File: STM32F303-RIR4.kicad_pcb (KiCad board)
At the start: 2 copper layers, 73.7 x 106.7 mm, 10 parts, among them J0 CN7, J1 CN10, J101 LCC, J102 LCC, U101 SN65HVD1050

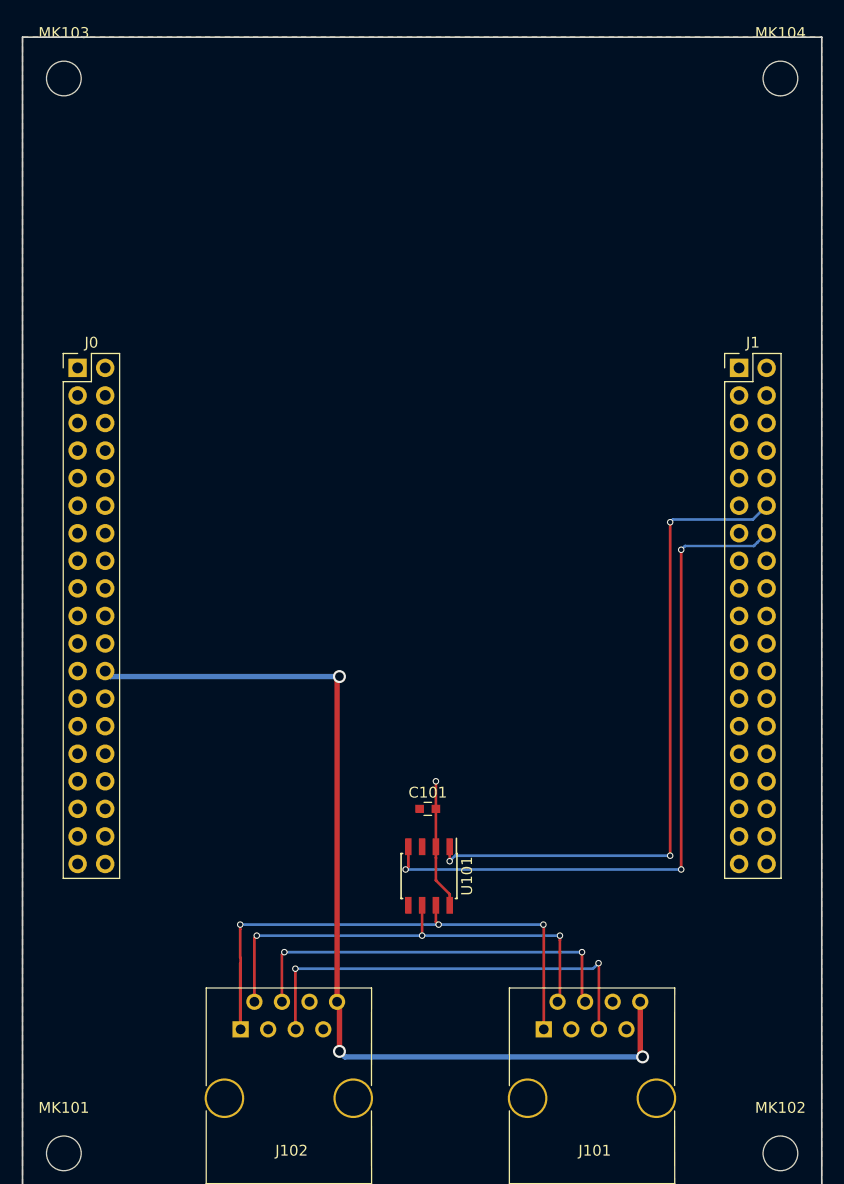
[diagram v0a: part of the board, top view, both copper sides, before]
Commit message: Add activity LEDS.
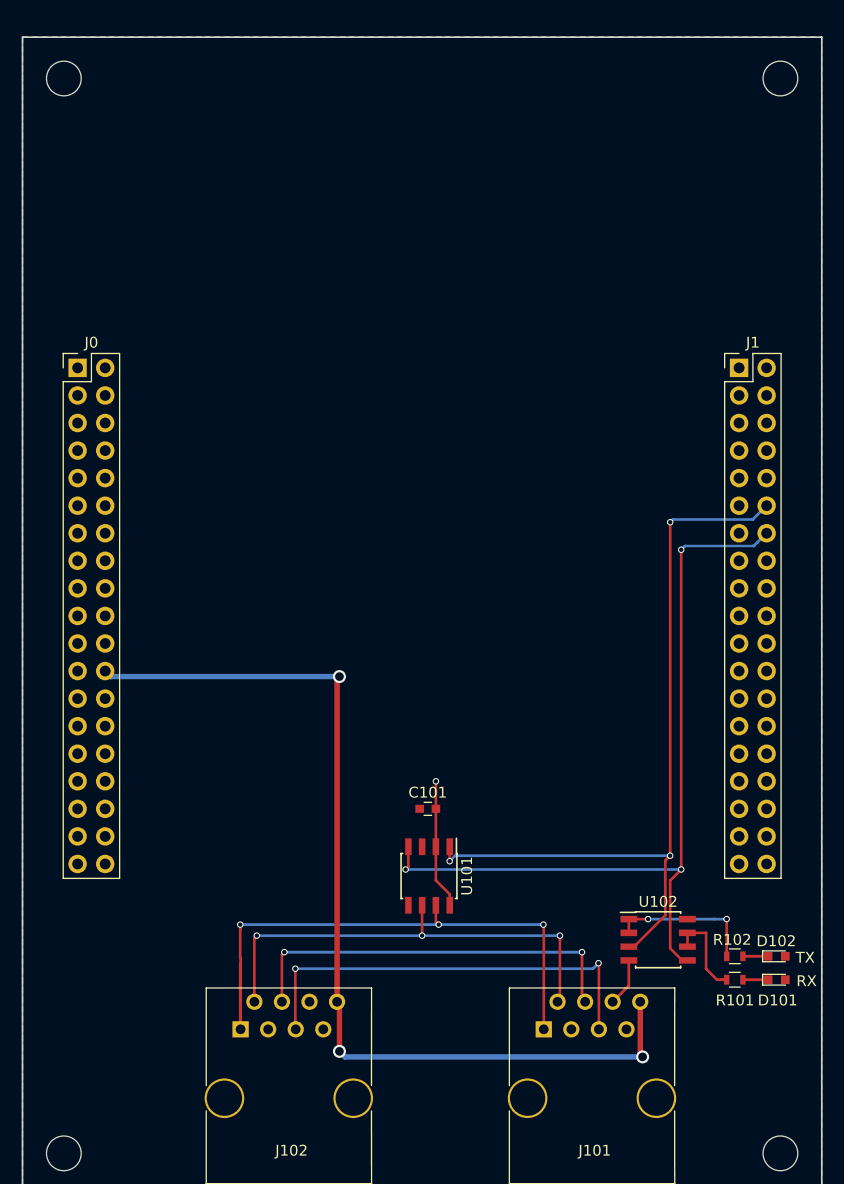
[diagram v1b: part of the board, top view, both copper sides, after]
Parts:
- added D101: RX, LEDs:LED_0603, F.Cu at (182.5, 158.0)
- added D102: TX, LEDs:LED_0603, F.Cu at (182.5, 155.8)
- added R101: 390, Resistors_SMD:R_0603, F.Cu at (178.7, 158.0)
- added R102: 390, Resistors_SMD:R_0603, F.Cu at (178.7, 155.8)
- added U102: LM358, Housings_SOIC:SOIC-8_3.9x4.9mm_Pitch1.27mm, F.Cu at (171.6, 154.3)
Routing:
- net Net-(R102-Pad2): track 0.00 -> 13.7 mm, vias 0 -> 2
- net /CAN_TX: track 62.1 -> 72.4 mm
- net /CAN_RX: track 65.6 -> 75.3 mm
- net Net-(R101-Pad2): track 0.00 -> 8.86 mm
- net GND: track 12.0 -> 16.4 mm
- net Net-(D102-Pad1): track 0.00 -> 2.31 mm
- net Net-(D101-Pad1): track 0.00 -> 2.31 mm

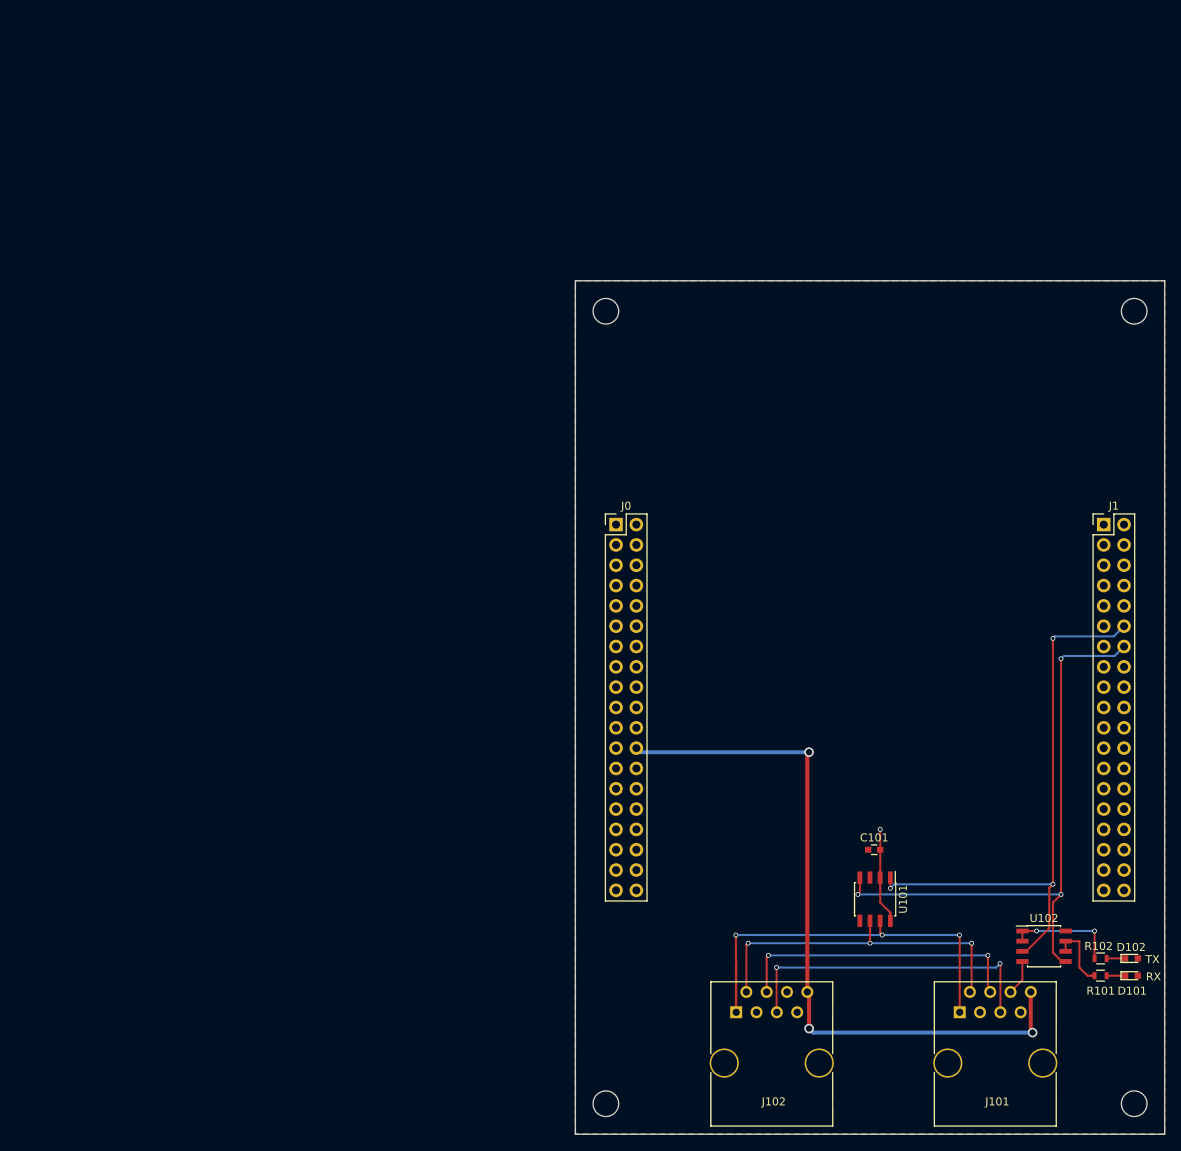
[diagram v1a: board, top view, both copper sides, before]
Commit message: Final tweaks to the board, added labels and logos.
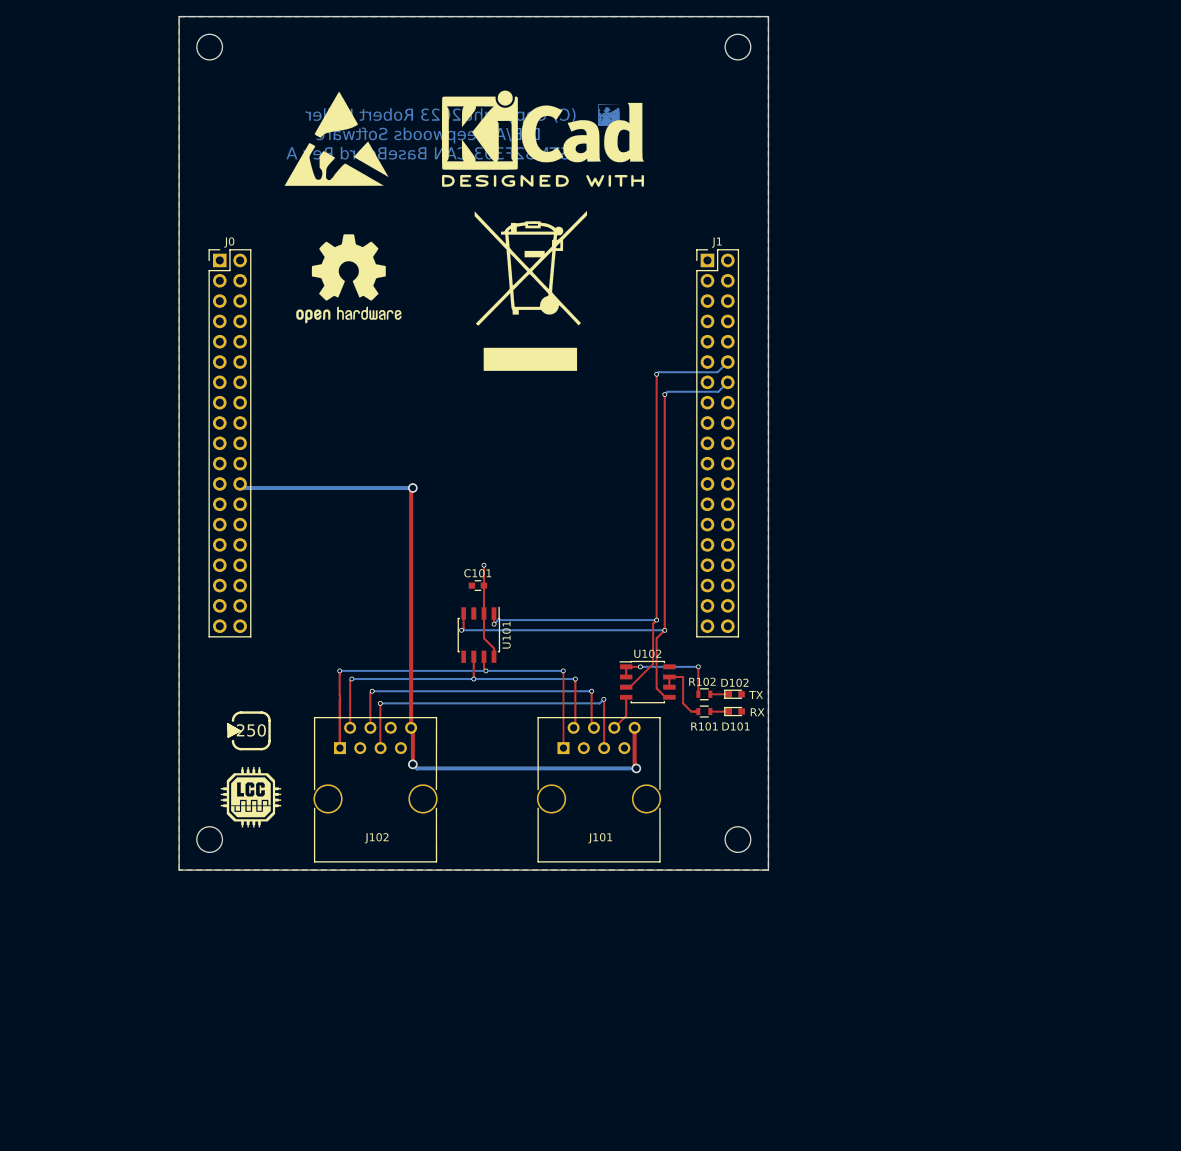
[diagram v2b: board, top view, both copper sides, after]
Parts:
- added ?: , DWSLogoBCU:DWSLogoBCU, F.Cu at (117.2, 50.4)
- added G***: LCC, LCC_LOGO:LCC_LOGO_9x9, F.Cu at (72.5, 135.6)
- added REF**: PowerLabel-250, PowerLabels:PowerLabel-250, F.Cu at (72.5, 127.4)
- added REF***: ESD-Logo_13.2x12mm_SilkScreen, Symbols:ESD-Logo_13.2x12mm_SilkScreen, F.Cu at (83.2, 53.3)
- added REF***: KiCad-Logo2_12mm_SilkScreen, Symbols:KiCad-Logo2_12mm_SilkScreen, F.Cu at (109.0, 53.3)
- added REF***: OSHW-Logo2_14.6x12mm_SilkScreen, Symbols:OSHW-Logo2_14.6x12mm_SilkScreen, F.Cu at (84.7, 70.9)
- added REF***: WEEE-Logo_14x20mm_SilkScreen, Symbols:WEEE-Logo_14x20mm_SilkScreen, F.Cu at (107.4, 72.4)
- moved U102 59.5 mm to (122.1, 121.3)
- moved C101 59.5 mm to (100.8, 109.2)
- moved D102 59.5 mm to (133.0, 122.8)
- moved J102 59.5 mm to (83.6, 129.5)
- moved MK101 59.5 mm to (67.3, 141.0)
- moved MK102 59.5 mm to (133.3, 141.0)
- moved MK103 59.5 mm to (67.3, 41.9)
- moved MK104 59.5 mm to (133.3, 41.9)
- moved R102 59.5 mm to (129.1, 122.8)
- moved U101 59.5 mm to (101.0, 115.4)
- moved J101 59.5 mm to (111.5, 129.5)
- moved D101 59.5 mm to (133.0, 125.0)
- moved J0 59.5 mm to (68.6, 68.6)
- moved J1 59.5 mm to (129.5, 68.6)
- moved R101 59.5 mm to (129.1, 125.0)
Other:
- board text added: "(C) Copyright 2023 Robert Heller D/B/A Deepwoods Software STM32F303 CAN BaseBoard Rev A"

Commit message: Add additional outputs (crossing controls).
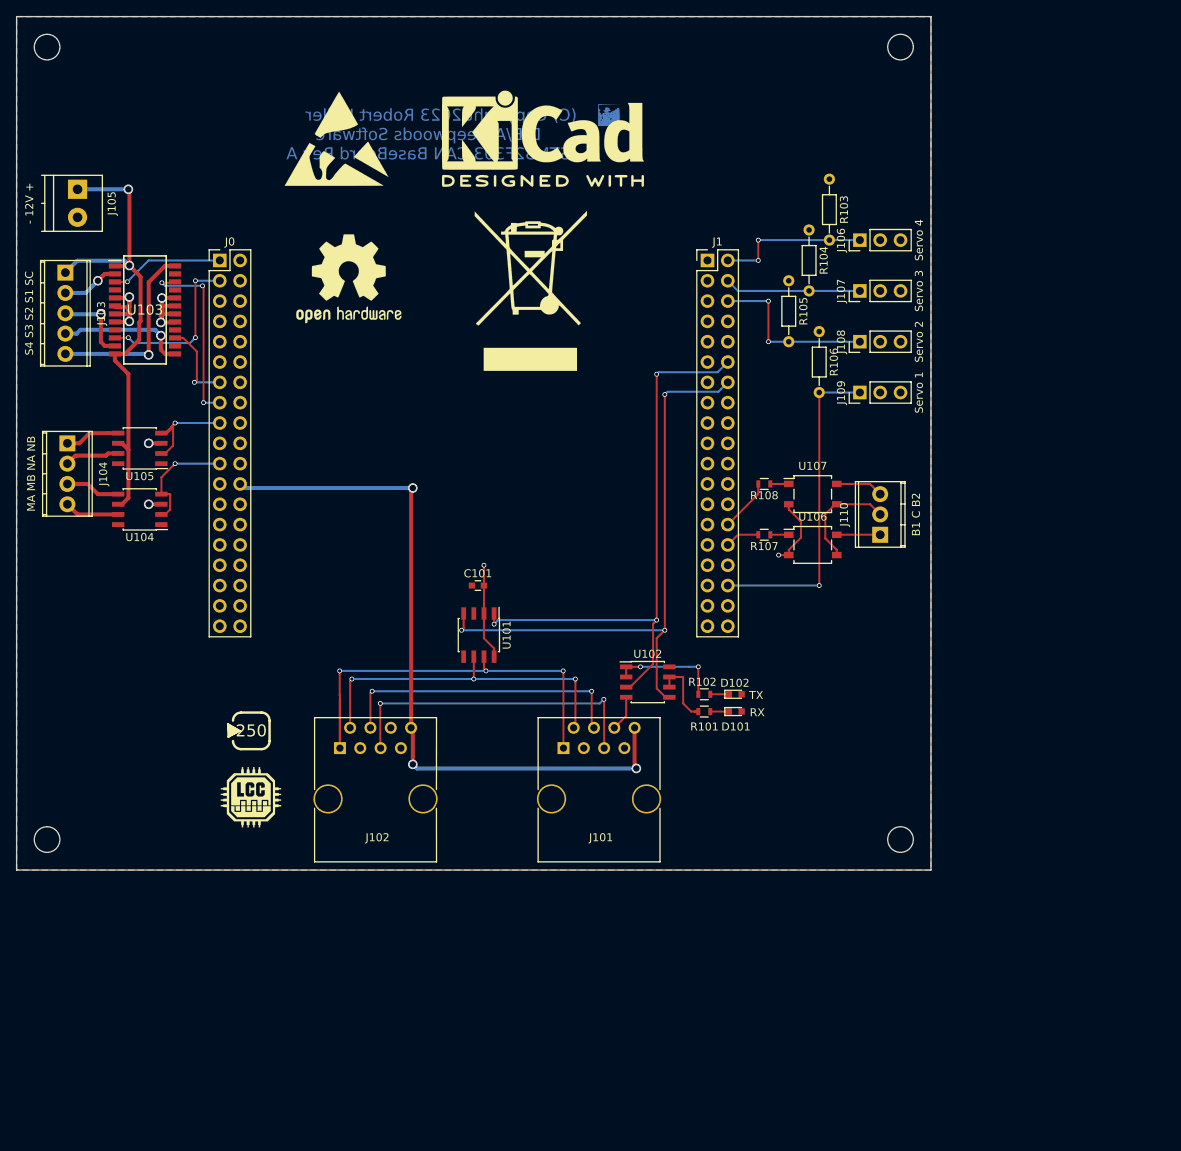
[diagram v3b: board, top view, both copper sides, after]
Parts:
- added J103: S4 S3 S2 S1 SC, Terminal_Blocks:TerminalBlock_Pheonix_MPT-2.54mm_5pol, F.Cu at (49.3, 70.1)
- added J104: MA MB NA NB, Terminal_Blocks:TerminalBlock_Pheonix_MPT-2.54mm_4pol, F.Cu at (49.5, 91.4)
- added J105: - 12V +, Terminal_Blocks:TerminalBlock_Pheonix_PT-3.5mm_2pol, F.Cu at (50.8, 59.7)
- added J106: Servo 4, Pin_Headers:Pin_Header_Straight_1x03_Pitch2.54mm, F.Cu at (148.6, 66.0)
- added J107: Servo 3, Pin_Headers:Pin_Header_Straight_1x03_Pitch2.54mm, F.Cu at (148.6, 72.4)
- added J108: Servo 2, Pin_Headers:Pin_Header_Straight_1x03_Pitch2.54mm, F.Cu at (148.6, 78.7)
- added J109: Servo 1, Pin_Headers:Pin_Header_Straight_1x03_Pitch2.54mm, F.Cu at (148.6, 85.1)
- added J110: B1 C B2, Terminal_Blocks:TerminalBlock_Pheonix_MPT-2.54mm_3pol, F.Cu at (151.1, 102.9)
- added R103: 5K to 20K, Resistors_THT:R_Axial_DIN0204_L3.6mm_D1.6mm_P7.62mm_Horizontal, F.Cu at (144.8, 58.4)
- added R104: 5K to 20K, Resistors_THT:R_Axial_DIN0204_L3.6mm_D1.6mm_P7.62mm_Horizontal, F.Cu at (142.2, 64.8)
- added R105: 5K to 20K, Resistors_THT:R_Axial_DIN0204_L3.6mm_D1.6mm_P7.62mm_Horizontal, F.Cu at (139.7, 71.1)
- added R106: 5K to 20K, Resistors_THT:R_Axial_DIN0204_L3.6mm_D1.6mm_P7.62mm_Horizontal, F.Cu at (143.5, 77.5)
- added R107: 330, Resistors_SMD:R_0603, F.Cu at (136.6, 102.9)
- added R108: 330, Resistors_SMD:R_0603, F.Cu at (136.6, 96.5)
- added U103: TBD62064AFG, SOP100P800X190:SOP100P800X190-24N, F.Cu at (59.2, 74.8)
- added U104: TC4428, Housings_SOIC:SOIC-8_3.9x4.9mm_Pitch1.27mm, F.Cu at (58.6, 99.7)
- added U105: TC4428, Housings_SOIC:SOIC-8_3.9x4.9mm_Pitch1.27mm, F.Cu at (58.6, 92.1)
- added U106: G3VM-61VY4, Housings_SOIC:SO-4_4.4x4.3mm_Pitch2.54mm, F.Cu at (142.7, 104.1)
- added U107: G3VM-61VY4, Housings_SOIC:SO-4_4.4x4.3mm_Pitch2.54mm, F.Cu at (142.7, 97.8)
- moved MK101 20.3 mm to (47.0, 141.0)
- moved MK103 20.3 mm to (47.0, 41.9)
- moved MK102 20.3 mm to (153.7, 141.0)
- moved MK104 20.3 mm to (153.7, 41.9)
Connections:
- J1 pad 2: Net-(J1-Pad2) -> /Servo4
- J1 pad 28: Net-(J1-Pad28) -> /SSR2
- J1 pad 30: Net-(J1-Pad30) -> /SSR1
- J1 pad 34: Net-(J1-Pad34) -> /Servo1
- J1 pad 4: Net-(J1-Pad4) -> /Servo3
- J1 pad 6: Net-(J1-Pad6) -> /Servo2
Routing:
- net +12V: track 0.00 -> 62.2 mm, vias 0 -> 2
- net /Servo1: track 0.00 -> 40.6 mm, vias 0 -> 1
- net GND: track 16.4 -> 55.1 mm, vias 1 -> 8
- net Net-(J103-Pad5): track 0.00 -> 23.7 mm, vias 0 -> 1
- net Net-(J0-Pad15): track 0.00 -> 23.6 mm, vias 0 -> 3
- net /Servo2: track 0.00 -> 21.6 mm, vias 0 -> 2
- net Net-(J0-Pad3): track 0.00 -> 20.8 mm, vias 0 -> 3
- net /Servo4: track 0.00 -> 19.0 mm, vias 0 -> 2
- net /Servo3: track 0.00 -> 17.0 mm
- net Net-(J103-Pad4): track 0.00 -> 16.2 mm, vias 0 -> 1
- net Net-(J0-Pad17): track 0.00 -> 14.6 mm, vias 0 -> 1
- net Net-(J0-Pad21): track 0.00 -> 14.4 mm, vias 0 -> 1
- net Net-(J0-Pad1): track 0.00 -> 14.2 mm, vias 0 -> 1
- net Net-(J110-Pad2): track 0.00 -> 13.6 mm
- net Net-(J0-Pad13): track 0.00 -> 10.6 mm, vias 0 -> 1
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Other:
- board size 73.7 x 106.7 mm -> 114.3 x 106.7 mm

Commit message: Update to new version.
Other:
- net class Default removed

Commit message: Assorted minor updates.
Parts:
- U103: footprint SOP100P800X190:SOP100P800X190-24N -> MyHSOP:HSOP16-P-300-1.00
- moved U103 0.50 mm to (59.1, 74.3), turned to -90 degrees
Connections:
- J0 pad 10: Net-(J0-Pad10) -> unconnected-(J0-Pad10)
- J0 pad 11: Net-(J0-Pad11) -> unconnected-(J0-Pad11)
- J0 pad 12: Net-(J0-Pad12) -> unconnected-(J0-Pad12)
- J0 pad 14: Net-(J0-Pad14) -> unconnected-(J0-Pad14)
- J0 pad 16: Net-(J0-Pad16) -> unconnected-(J0-Pad16)
- J0 pad 2: Net-(J0-Pad2) -> unconnected-(J0-Pad2)
- J0 pad 23: Net-(J0-Pad23) -> unconnected-(J0-Pad23)
- J0 pad 25: Net-(J0-Pad25) -> unconnected-(J0-Pad25)
- J0 pad 26: Net-(J0-Pad26) -> unconnected-(J0-Pad26)
- J0 pad 27: Net-(J0-Pad27) -> unconnected-(J0-Pad27)
- J0 pad 28: Net-(J0-Pad28) -> unconnected-(J0-Pad28)
- J0 pad 29: Net-(J0-Pad29) -> unconnected-(J0-Pad29)
- J0 pad 30: Net-(J0-Pad30) -> unconnected-(J0-Pad30)
- J0 pad 31: Net-(J0-Pad31) -> unconnected-(J0-Pad31)
- J0 pad 32: Net-(J0-Pad32) -> unconnected-(J0-Pad32)
- J0 pad 33: Net-(J0-Pad33) -> unconnected-(J0-Pad33)
- J0 pad 34: Net-(J0-Pad34) -> unconnected-(J0-Pad34)
- J0 pad 35: Net-(J0-Pad35) -> unconnected-(J0-Pad35)
- J0 pad 36: Net-(J0-Pad36) -> unconnected-(J0-Pad36)
- J0 pad 37: Net-(J0-Pad37) -> unconnected-(J0-Pad37)
- J0 pad 38: Net-(J0-Pad38) -> unconnected-(J0-Pad38)
- J0 pad 4: Net-(J0-Pad4) -> unconnected-(J0-Pad4)
- J0 pad 5: Net-(J0-Pad5) -> unconnected-(J0-Pad5)
- J0 pad 6: Net-(J0-Pad6) -> unconnected-(J0-Pad6)
- J0 pad 7: Net-(J0-Pad7) -> unconnected-(J0-Pad7)
- J0 pad 9: Net-(J0-Pad9) -> unconnected-(J0-Pad9)
- J1 pad 1: Net-(J1-Pad1) -> unconnected-(J1-Pad1)
- J1 pad 10: Net-(J1-Pad10) -> unconnected-(J1-Pad10)
- J1 pad 11: Net-(J1-Pad11) -> unconnected-(J1-Pad11)
- J1 pad 13: Net-(J1-Pad13) -> unconnected-(J1-Pad13)
- J1 pad 15: Net-(J1-Pad15) -> unconnected-(J1-Pad15)
- J1 pad 16: Net-(J1-Pad16) -> unconnected-(J1-Pad16)
- J1 pad 17: Net-(J1-Pad17) -> unconnected-(J1-Pad17)
- J1 pad 18: Net-(J1-Pad18) -> unconnected-(J1-Pad18)
- J1 pad 19: Net-(J1-Pad19) -> unconnected-(J1-Pad19)
- J1 pad 21: Net-(J1-Pad21) -> unconnected-(J1-Pad21)
- J1 pad 22: Net-(J1-Pad22) -> unconnected-(J1-Pad22)
- J1 pad 23: Net-(J1-Pad23) -> unconnected-(J1-Pad23)
- J1 pad 24: Net-(J1-Pad24) -> unconnected-(J1-Pad24)
- J1 pad 25: Net-(J1-Pad25) -> unconnected-(J1-Pad25)
- J1 pad 26: Net-(J1-Pad26) -> unconnected-(J1-Pad26)
- J1 pad 27: Net-(J1-Pad27) -> unconnected-(J1-Pad27)
- J1 pad 29: Net-(J1-Pad29) -> unconnected-(J1-Pad29)
- J1 pad 3: Net-(J1-Pad3) -> unconnected-(J1-Pad3)
- J1 pad 31: Net-(J1-Pad31) -> unconnected-(J1-Pad31)
- J1 pad 33: Net-(J1-Pad33) -> unconnected-(J1-Pad33)
- J1 pad 35: Net-(J1-Pad35) -> unconnected-(J1-Pad35)
- J1 pad 36: Net-(J1-Pad36) -> unconnected-(J1-Pad36)
- J1 pad 37: Net-(J1-Pad37) -> unconnected-(J1-Pad37)
- J1 pad 38: Net-(J1-Pad38) -> unconnected-(J1-Pad38)
- J1 pad 5: Net-(J1-Pad5) -> unconnected-(J1-Pad5)
- J1 pad 8: Net-(J1-Pad8) -> unconnected-(J1-Pad8)
- U101 pad 5: Net-(U101-Pad5) -> unconnected-(U101-Pad5)
- U103 pad 10: Net-(J0-Pad3) -> (no net)
- U103 pad 11: Net-(J103-Pad3) -> Net-(J0-Pad13)
- U103 pad 12: +12V -> (no net)
- U103 pad 13: Net-(J103-Pad4) -> Net-(J103-Pad5)
- U103 pad 14: (no net) -> Net-(J0-Pad15)
- U103 pad 15: Net-(J0-Pad13) -> (no net)
- U103 pad 5: GND -> (no net)
- U103 pad 6: GND -> Net-(J0-Pad3)
- U103 pad 7: GND -> Net-(J103-Pad3)
- U103 pad 8: GND -> +12V
- U103 pad 9: (no net) -> Net-(J103-Pad4)
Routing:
- net GND: track 55.1 -> 38.6 mm, vias 8 -> 12
- net Net-(J101-Pad1): track 55.2 -> 49.2 mm
- net +12V: track 62.2 -> 68.3 mm
- net Net-(J0-Pad15): track 23.6 -> 21.9 mm
- net Net-(J103-Pad5): track 23.7 -> 22.4 mm, vias 1 -> 3
- net Net-(J103-Pad2): track 7.18 -> 8.25 mm
- net Net-(J103-Pad3): track 9.91 -> 9.15 mm
- net Net-(J103-Pad4): track 16.2 -> 16.8 mm

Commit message: Prep for PCB making.
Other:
- rule pad_to_mask_clearance: 0.2 -> 0.05

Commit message: Prep for PCB making.
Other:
- rule pad_to_mask_clearance: 0.05 -> 0
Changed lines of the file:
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@@
   )
   (setup
-    (pad_to_mask_clearance 0.05)
+    (pad_to_mask_clearance 0)
     (pcbplotparams
       (layerselection 0x0000030_80000001)
